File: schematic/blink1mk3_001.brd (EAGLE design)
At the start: 13.2 x 13.7 mm, 13 parts, among them U2 EFM32HG309F64G, X1 USB

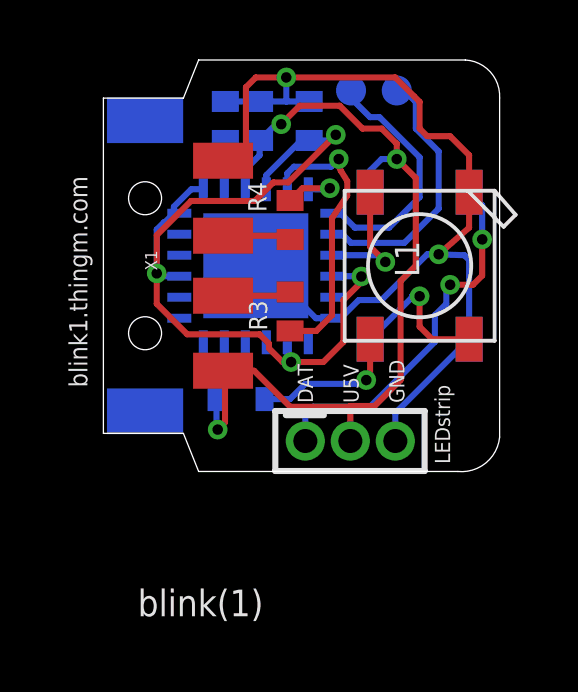
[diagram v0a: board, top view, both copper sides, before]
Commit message: fix DI pin so it does not badly interact with tomu firmware
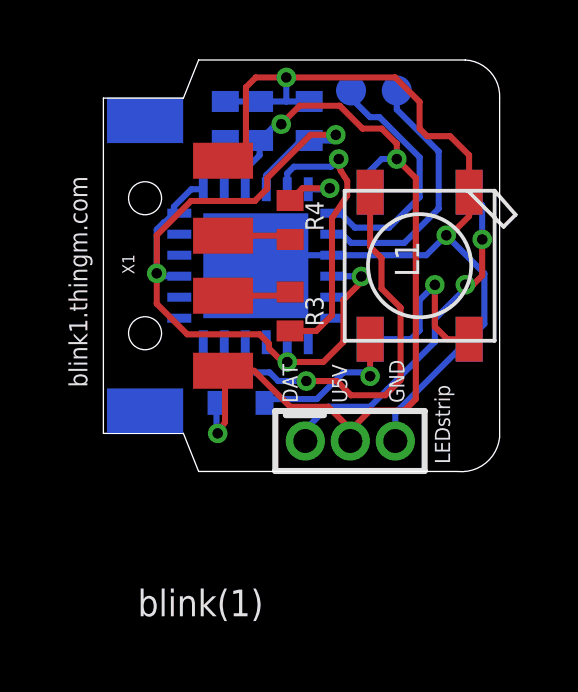
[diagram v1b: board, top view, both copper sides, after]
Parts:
- moved D1 0.13 mm to (3.17, -4.57)
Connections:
- net N$4 renamed CAP1A
- removed net LED0: U2.5
- new net CAP1B: U2.24
- net DI: now also U2.5; no longer U2.21
- net GND: now also U2.21; no longer U2.24
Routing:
- net DI: track 4.39 -> 13.8 mm
- net N$2: track 5.32 -> 6.43 mm
- net GND: track 36.2 -> 35.3 mm
- net DO: track 12.5 -> 11.9 mm
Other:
- board text added: "blink1mk3_001"
- board text removed: "blink1mk2_tomu"

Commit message: moved decoupling caps because of bottomside front support
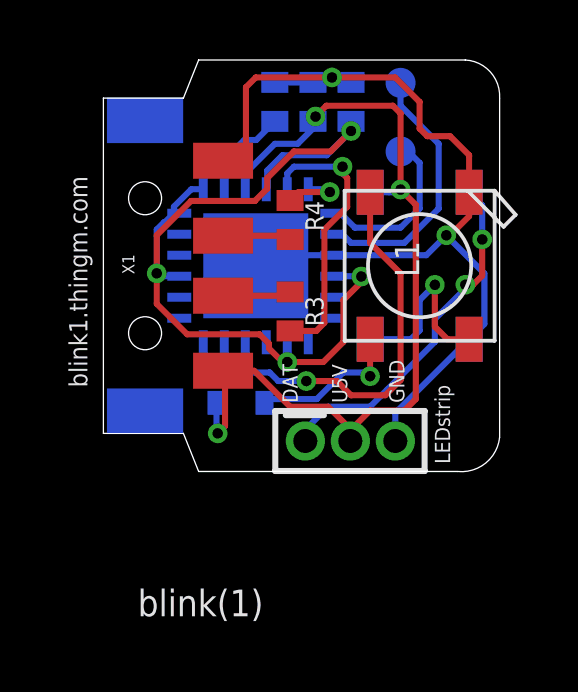
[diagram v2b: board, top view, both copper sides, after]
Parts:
- moved C 2.62 mm to (8.51, 3.81)
- moved C6 1.89 mm to (5.59, 5.46)
- moved C4 1.77 mm to (4.32, 5.46)
- moved C5 1.53 mm to (6.86, 5.46)
- moved D 0.28 mm to (8.51, 6.10)
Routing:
- net DBG_SWCLK: track 8.22 -> 5.69 mm
- net DECOUPLE: track 1.64 -> 3.43 mm
- net +3V3: track 29.4 -> 30.9 mm

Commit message: better pcb layout
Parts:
- D1: device adafruit:SOD-523 -> diode:SOD523
- moved D1 0.13 mm to (3.17, -4.70), turned to 0 degrees
- renumbered U2 to U1
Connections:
- net VLEDA: now also D1.C; no longer D1.K

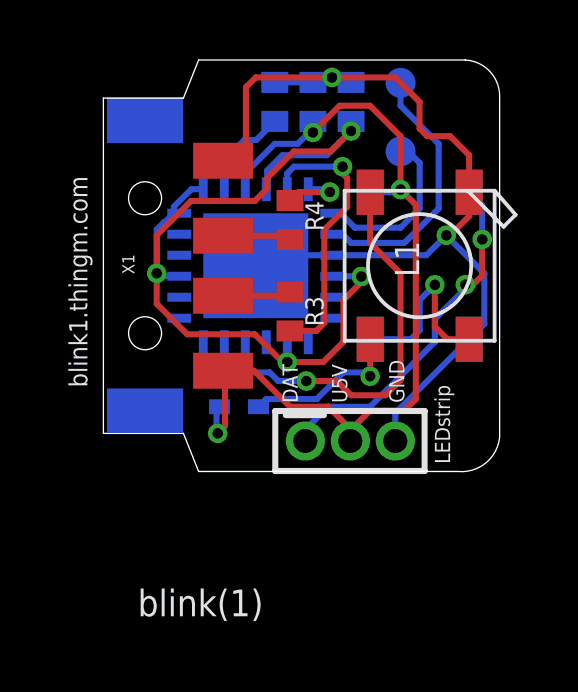
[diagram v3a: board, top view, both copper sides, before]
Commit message: version submitted to oshpark
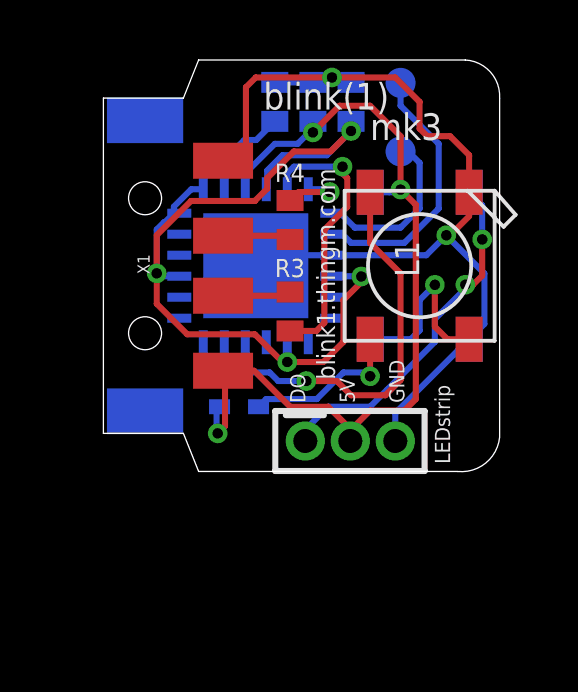
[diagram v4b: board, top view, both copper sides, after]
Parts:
- D1: value (none) -> 1N1418
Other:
- board text added: "5V"
- board text added: "DO"
- board text added: "mk3"
- board text removed: "DAT"
- board text removed: "U5V"
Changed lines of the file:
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@@
 <layer number="14" name="Route14" color="1" fill="6" visible="no" active="yes"/>
 <layer number="15" name="Route15" color="4" fill="6" visible="no" active="yes"/>
-<layer number="16" name="Bottom" color="3" fill="1" visible="yes" active="yes"/>
+<layer number="16" name="Bottom" color="3" fill="1" visible="no" active="yes"/>
 <layer number="17" name="Pads" color="2" fill="1" visible="yes" active="yes"/>
 <layer number="18" name="Vias" color="2" fill="1" visible="yes" active="yes"/>
@@
 <layer number="20" name="Dimension" color="15" fill="1" visible="yes" active="yes"/>
 <layer number="21" name="tPlace" color="7" fill="1" visible="yes" active="yes"/>
-<layer number="22" name="bPlace" color="7" fill="1" visible="yes" active="yes"/>
+<layer number="22" name="bPlace" color="7" fill="1" visible="no" active="yes"/>
 <layer number="23" name="tOrigins" color="15" fill="1" visible="yes" active="yes"/>
-<layer number="24" name="bOrigins" color="15" fill="1" visible="yes" active="yes"/>
+<layer number="24" name="bOrigins" color="15" fill="1" visible="no" active="yes"/>
 <layer number="25" name="tNames" color="7" fill="1" visible="yes" active="yes"/>
-<layer number="26" name="bNames" color="7" fill="1" visible="yes" active="yes"/>
+<layer number="26" name="bNames" color="7" fill="1" visible="no" active="yes"/>
 <layer number="27" name="tValues" color="7" fill="1" visible="no" active="yes"/>
 <layer number="28" name="bValues" color="7" fill="1" visible="no" active="yes"/>
@@
 <layer number="38" name="bTest" color="7" fill="1" visible="no" active="yes"/>
 <layer number="39" name="tKeepout" color="4" fill="11" visible="yes" active="yes"/>
-<layer number="40" name="bKeepout" color="1" fill="11" visible="yes" active="yes"/>
+<layer number="40" name="bKeepout" color="1" fill="11" visible="no" active="yes"/>
 <layer number="41" name="tRestrict" color="4" fill="10" visible="yes" active="yes"/>
-<layer number="42" name="bRestrict" color="1" fill="10" visible="yes" active="yes"/>
+<layer number="42" name="bRestrict" color="1" fill="10" visible="no" active="yes"/>
 <layer number="43" name="vRestrict" color="2" fill="10" visible="no" active="yes"/>
 <layer number="44" name="Drills" color="7" fill="1" visible="no" active="yes"/>
@@
 <layer number="50" name="dxf" color="7" fill="1" visible="no" active="yes"/>
 <layer number="51" name="tDocu" color="7" fill="1" visible="yes" active="yes"/>
-<layer number="52" name="bDocu" color="7" fill="1" visible="yes" active="yes"/>
+<layer number="52" name="bDocu" color="7" fill="1" visible="no" active="yes"/>
 <layer number="53" name="tGND_GNDA" color="7" fill="9" visible="no" active="no"/>
 <layer number="54" name="bGND_GNDA" color="1" fill="9" visible="no" active="no"/>
@@
 <board>
 <plain>
-<text x="-1.9304" y="-4.0539" size="0.6096" layer="21" ratio="10" rot="SR90">blink1.thingm.com</text>
-<text x="-0.254" y="-11.684" size="0.889" layer="21" ratio="10">blink(1)</text>
-<text x="-1.016" y="-3.81" size="0.6096" layer="22" ratio="10" rot="MR90">blink1mk3_001</text>
+<text x="6.3246" y="-3.7999" size="0.6096" layer="21" ratio="12" rot="SR90">blink1.thingm.com</text>
+<text x="3.937" y="5.207" size="0.889" layer="21" ratio="12">blink(1)</text>
+<text x="-1.143" y="-3.556" size="0.6096" layer="22" ratio="10" rot="MR90">blink1mk3_001</text>
 <rectangle x1="8.3407" y1="12.3031" x2="10.2457" y2="12.3095" layer="200"/>
 <rectangle x1="8.3407" y1="12.3095" x2="10.2457" y2="12.3158" layer="200"/>
@@
 <rectangle x1="8.3407" y1="14.1954" x2="10.2457" y2="14.2018" layer="200"/>
 <rectangle x1="8.3407" y1="14.2018" x2="10.2457" y2="14.2081" layer="200"/>
-<text x="5.08" y="-4.572" size="0.508" layer="21" ratio="10" rot="R90">DAT</text>
-<text x="6.731" y="-4.572" size="0.508" layer="21" ratio="10" rot="R90">U5V</text>
+<text x="5.334" y="-4.572" size="0.508" layer="21" ratio="10" rot="R90">DO</text>
+<text x="6.985" y="-4.572" size="0.508" layer="21" ratio="10" rot="R90">5V</text>
 <text x="8.636" y="-4.572" size="0.508" layer="21" ratio="10" rot="R90">GND</text>
 <wire x1="-1.397" y1="5.588" x2="1.27" y2="5.588" width="0" layer="20"/>
@@
 <wire x1="-1.397" y1="5.588" x2="-1.397" y2="-5.588" width="0" layer="20"/>
 <wire x1="-2.54" y1="0" x2="16.51" y2="0" width="0" layer="48"/>
-<text x="10.16" y="-6.604" size="0.508" layer="21" ratio="10" rot="R90">LEDstrip</text>
+<text x="10.16" y="-6.604" size="0.508" layer="21" ratio="12" rot="R90">LEDstrip</text>
 <dimension x1="10.668" y1="-6.858" x2="10.668" y2="6.858" x3="13.97" y3="0" textsize="0.6096" layer="48" dtype="vertical" width="0.0762" unit="inch" visible="yes"/>
 <dimension x1="-1.397" y1="5.588" x2="11.811" y2="5.08" x3="5.207" y3="8.128" textsize="0.6096" layer="48" dtype="horizontal" width="0.0762" unit="inch" visible="yes"/>
@@
 <vertex x="3.429" y="7.239"/>
 </polygon>
+<text x="7.493" y="4.191" size="0.889" layer="21" ratio="12">mk3</text>
 </plain>
 <attributes>
@@
 <elements>
 <element name="X1" library="todstuff" package="MOLEX-48037-1000" value="USB" x="-0.008" y="0" smashed="yes">
-<attribute name="NAME" x="-0.77" y="0.381" size="0.4064" layer="25" font="vector" ratio="10" rot="R270"/>
+<attribute name="NAME" x="-0.262" y="0.381" size="0.4064" layer="25" font="vector" ratio="10" rot="R270"/>
 <attribute name="VALUE" x="-4.056" y="-1.524" size="1.27" layer="27" font="vector" rot="R90"/>
 </element>
@@
 <element name="JP3" library="todstuff" package="1X03-1.5MM" value="M03MM" x="5.334" y="-5.842" smashed="yes"/>
 <element name="U1" library="todstuff" package="QFN24PAD" value="EFM32HG309F64G" x="3.683" y="0" smashed="yes" rot="MR90">
-<attribute name="NAME" x="7.136" y="-3.576" size="0.8128" layer="26" ratio="12" rot="MR0"/>
+<attribute name="NAME" x="5.437" y="-2.647" size="0.8128" layer="26" ratio="12" rot="MR180"/>
 <attribute name="VALUE" x="-1.759" y="-2.868" size="1.27" layer="28" rot="MR90"/>
 </element>
 <element name="C4" library="adafruit" library_urn="urn:adsk.eagle:library:420" package="C0402" value="1uF" x="4.318" y="5.461" smashed="yes" rot="MR90">
-<attribute name="NAME" x="4.572" y="3.81" size="0.6096" layer="26" ratio="12" rot="MR0"/>
+<attribute name="NAME" x="4.572" y="3.683" size="0.6096" layer="26" ratio="12" rot="MR0"/>
 <attribute name="VALUE" x="2.868" y="4.961" size="1.016" layer="28" rot="MR90"/>
 </element>
 <element name="C5" library="adafruit" library_urn="urn:adsk.eagle:library:420" package="C0402" value="1uF" x="6.858" y="5.461" smashed="yes" rot="MR90">
-<attribute name="NAME" x="7.366" y="3.81" size="0.6096" layer="26" ratio="12" rot="MR0"/>
+<attribute name="NAME" x="7.366" y="3.683" size="0.6096" layer="26" ratio="12" rot="MR0"/>
 <attribute name="VALUE" x="4.953" y="4.826" size="1.27" layer="28" rot="MR90"/>
 </element>
 <element name="C6" library="adafruit" library_urn="urn:adsk.eagle:library:420" package="C0402" value="4.7uF" x="5.588" y="5.461" smashed="yes" rot="MR90">
-<attribute name="NAME" x="5.969" y="3.81" size="0.6096" layer="26" ratio="12" rot="MR0"/>
+<attribute name="NAME" x="5.969" y="3.683" size="0.6096" layer="26" ratio="12" rot="MR0"/>
 <attribute name="VALUE" x="3.683" y="4.826" size="1.27" layer="28" rot="MR90"/>
 </element>
 <element name="R3" library="adafruit" library_urn="urn:adsk.eagle:library:420" package="R0402" value="15" x="4.826" y="-1.524" smashed="yes" rot="R90">
-<attribute name="NAME" x="5.334" y="-1.016" size="0.6096" layer="25" ratio="12" rot="R270"/>
+<attribute name="NAME" x="4.318" y="-0.381" size="0.6096" layer="25" ratio="12"/>
 <attribute name="VALUE" x="6.858" y="-2.159" size="1.27" layer="27" rot="R90"/>
 </element>
 <element name="R4" library="adafruit" library_urn="urn:adsk.eagle:library:420" package="R0402" value="15" x="4.826" y="1.524" smashed="yes" rot="R270">
-<attribute name="NAME" x="5.334" y="2.159" size="0.6096" layer="25" ratio="12" rot="R270"/>
+<attribute name="NAME" x="4.318" y="2.794" size="0.6096" layer="25" ratio="12"/>
 <attribute name="VALUE" x="2.794" y="2.159" size="1.27" layer="27" rot="R270"/>
 </element>
@@
 <attribute name="VALUE" x="8.89" y="3.302" size="0.0254" layer="28" rot="MR0"/>
 </element>
-<element name="D1" library="diode" library_urn="urn:adsk.eagle:library:210" package="SOD523" package3d_urn="urn:adsk.eagle:package:43410/1" value="" x="3.175" y="-4.699" smashed="yes" rot="MR0">
+<element name="D1" library="diode" library_urn="urn:adsk.eagle:library:210" package="SOD523" package3d_urn="urn:adsk.eagle:package:43410/1" value="1N1418" x="3.175" y="-4.699" smashed="yes" rot="MR0">
 <attribute name="NAME" x="3.683" y="-5.842" size="0.6096" layer="26" ratio="12" rot="MR0"/>
 <attribute name="VALUE" x="3.81" y="-6.604" size="1.27" layer="28" rot="MR0"/>
